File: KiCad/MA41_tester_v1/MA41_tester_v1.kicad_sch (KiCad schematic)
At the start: 5 parts

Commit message: ...
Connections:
- net GND: now also A?.29 (GND), J?.1 (Pin_1)
- net MA41_UART_RX: now reaches J?.2 (Pin_2)
- net MA41_UART_TX: now reaches J?.3 (Pin_3)
- net +3.3V: now reaches J?.4 (Pin_4)
- net MA-41/VCC: now reaches A?.27 (+5V)
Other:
- sheet LCD ports: added GND, SCL, SDA, VCC; removed none
- sheet MA-41 ports: added 3.3V, GND, UART_RX, UART_TX, VCC; removed none
- moved on the sheet: A?, J?, R?

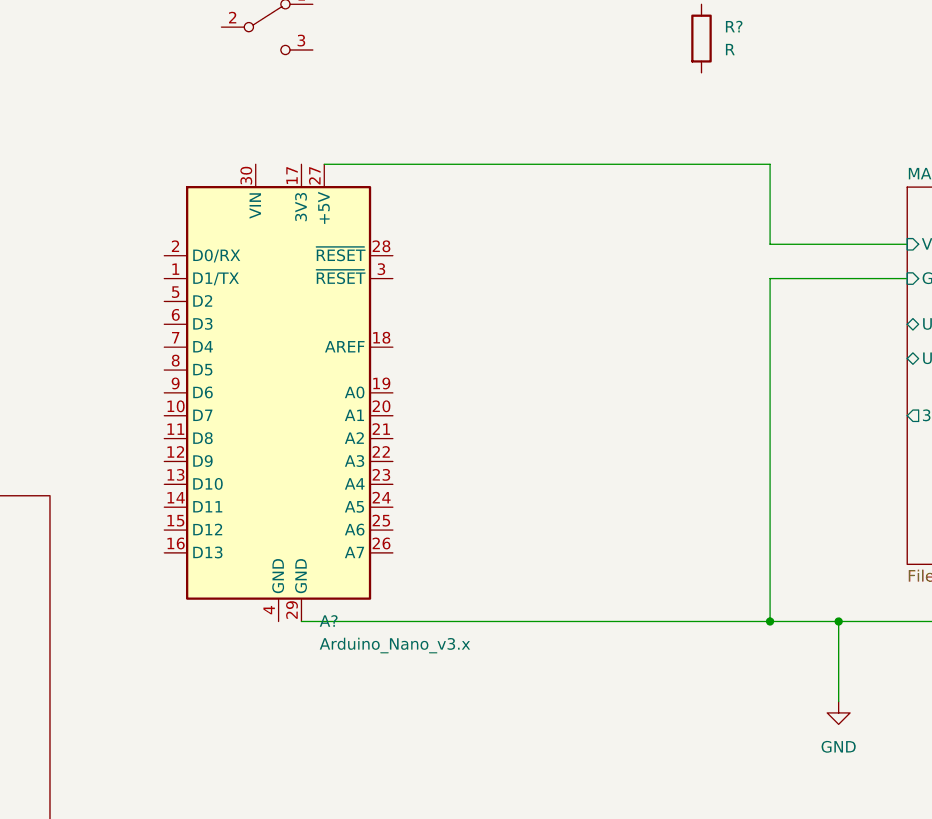
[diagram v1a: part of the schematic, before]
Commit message: arduino changed to esp32
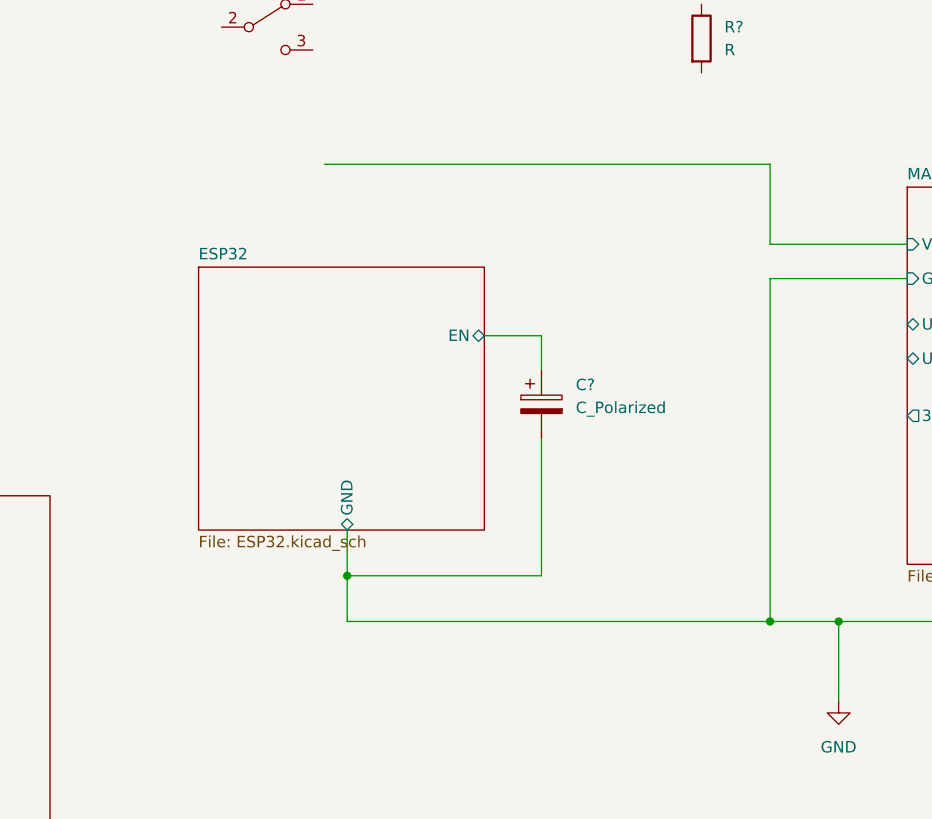
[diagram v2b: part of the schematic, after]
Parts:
- removed A?: Arduino_Nano_v3.x, Module:Arduino_Nano, symbol MCU_Module:Arduino_Nano_v3.x
- added C?: C_Polarized, symbol Device:C_Polarized
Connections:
- net GND: now also C?.2
- new net ESP32/EN: C?.1
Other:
- added sheet ESP32 (ESP32.kicad_sch)
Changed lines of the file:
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@@
   (junction (at 171.45 116.84) (diameter 0) (color 0 0 0 0)
   )
+  (junction (at 124.46 111.76) (diameter 0) (color 0 0 0 0)
+  )
   (junction (at 242.57 81.28) (diameter 0) (color 0 0 0 0)
   )
@@
     (stroke (width 0) (type default) (color 0 0 0 0))
   )
+  (wire (pts (xy 124.46 106.68) (xy 124.46 111.76))
+    (stroke (width 0) (type default) (color 0 0 0 0))
+  )
   (wire (pts (xy 251.46 80.01) (xy 251.46 78.74))
     (stroke (width 0) (type default) (color 0 0 0 0))
   )
+  (wire (pts (xy 124.46 111.76) (xy 124.46 116.84))
+    (stroke (width 0) (type default) (color 0 0 0 0))
+  )
   (wire (pts (xy 262.89 68.58) (xy 250.19 68.58))
     (stroke (width 0) (type default) (color 0 0 0 0))
@@
     (stroke (width 0) (type default) (color 0 0 0 0))
   )
+  (wire (pts (xy 139.7 85.09) (xy 146.05 85.09))
+    (stroke (width 0) (type default) (color 0 0 0 0))
+  )
   (wire (pts (xy 251.46 78.74) (xy 242.57 78.74))
     (stroke (width 0) (type default) (color 0 0 0 0))
@@
     (stroke (width 0) (type default) (color 0 0 0 0))
   )
+  (wire (pts (xy 146.05 96.52) (xy 146.05 111.76))
+    (stroke (width 0) (type default) (color 0 0 0 0))
+  )
+  (wire (pts (xy 146.05 111.76) (xy 124.46 111.76))
+    (stroke (width 0) (type default) (color 0 0 0 0))
+  )
   (wire (pts (xy 232.41 81.28) (xy 232.41 116.84))
     (stroke (width 0) (type default) (color 0 0 0 0))
@@
     (stroke (width 0) (type default) (color 0 0 0 0))
   )
-  (wire (pts (xy 119.38 116.84) (xy 171.45 116.84))
-    (stroke (width 0) (type default) (color 0 0 0 0))
-  )
   (wire (pts (xy 171.45 116.84) (xy 171.45 78.74))
     (stroke (width 0) (type default) (color 0 0 0 0))
@@
     (stroke (width 0) (type default) (color 0 0 0 0))
   )
+  (wire (pts (xy 146.05 85.09) (xy 146.05 88.9))
+    (stroke (width 0) (type default) (color 0 0 0 0))
+  )
   (wire (pts (xy 242.57 81.28) (xy 232.41 81.28))
+    (stroke (width 0) (type default) (color 0 0 0 0))
+  )
+  (wire (pts (xy 124.46 116.84) (xy 171.45 116.84))
     (stroke (width 0) (type default) (color 0 0 0 0))
   )
@@
     (pin "3")
   )
+  (symbol (lib_id "Device:C_Polarized") (at 146.05 92.71 0) (unit 1)
+    (in_bom yes) (on_board yes) (fields_autoplaced)
+    (property "Reference" "C?" (id 0) (at 149.86 90.5509 0)
+      (effects (font (size 1.27 1.27)) (justify left))
+    )
+    (property "Value" "C_Polarized" (id 1) (at 149.86 93.0909 0)
+      (effects (font (size 1.27 1.27)) (justify left))
+    )
+    (property "Footprint" "" (id 2) (at 147.0152 96.52 0)
+      (effects (font (size 1.27 1.27)) hide)
+    )
+    (property "Datasheet" "~" (id 3) (at 146.05 92.71 0)
+      (effects (font (size 1.27 1.27)) hide)
+    )
+    (pin "1")
+    (pin "2")
+  )
   (symbol (lib_id "Device:R") (at 163.83 52.07 0) (unit 1)
     (in_bom yes) (on_board yes) (fields_autoplaced)
@@
     (pin "2")
   )
-  (symbol (lib_id "MCU_Module:Arduino_Nano_v3.x") (at 116.84 91.44 0) (unit 1)
-    (in_bom yes) (on_board yes) (fields_autoplaced)
-    (property "Reference" "A?" (id 0) (at 121.3994 116.84 0)
-      (effects (font (size 1.27 1.27)) (justify left))
-    )
-    (property "Value" "Arduino_Nano_v3.x" (id 1) (at 121.3994 119.38 0)
-      (effects (font (size 1.27 1.27)) (justify left))
-    )
-    (property "Footprint" "Module:Arduino_Nano" (id 2) (at 116.84 91.44 0)
-      (effects (font (size 1.27 1.27) italic) hide)
-    )
-    (property "Datasheet" "http://www.mouser.com/pdfdocs/Gravitech_Arduino_Nano3_0.pdf" (id 3) (at 116.84 91.44 0)
-      (effects (font (size 1.27 1.27)) hide)
-    )
-    (pin "1")
-    (pin "10")
-    (pin "11")
-    (pin "12")
-    (pin "13")
-    (pin "14")
-    (pin "15")
-    (pin "16")
-    (pin "17")
-    (pin "18")
-    (pin "19")
-    (pin "2")
-    (pin "20")
-    (pin "21")
-    (pin "22")
-    (pin "23")
-    (pin "24")
-    (pin "25")
-    (pin "26")
-    (pin "27")
-    (pin "28")
-    (pin "29")
-    (pin "3")
-    (pin "30")
-    (pin "4")
-    (pin "5")
-    (pin "6")
-    (pin "7")
-    (pin "8")
-    (pin "9")
+  (sheet (at 107.95 77.47) (size 31.75 29.21) (fields_autoplaced)
+    (stroke (width 0.1524) (type solid) (color 0 0 0 0))
+    (fill (color 0 0 0 0.0000))
+    (property "Sheet name" "ESP32" (id 0) (at 107.95 76.7584 0)
+      (effects (font (size 1.27 1.27)) (justify left bottom))
+    )
+    (property "Sheet file" "ESP32.kicad_sch" (id 1) (at 107.95 107.2646 0)
+      (effects (font (size 1.27 1.27)) (justify left top))
+    )
+    (pin "EN" bidirectional (at 139.7 85.09 0)
+      (effects (font (size 1.27 1.27)) (justify right))
+    )
+    (pin "GND" bidirectional (at 124.46 106.68 270)
+      (effects (font (size 1.27 1.27)) (justify left))
+    )
   )
   (sheet (at 186.69 68.58) (size 29.21 41.91) (fields_autoplaced)
@@
     (path "/ec9ad0ca-c047-4fdf-90a6-0d80c2e2fb95" (page "2"))
     (path "/c0024dd4-f568-4a9d-af4a-b140e2a5476d" (page "3"))
+    (path "/0079f128-ad52-4f7c-b867-0c198ef9053a" (page "4"))
   )
   (symbol_instances
@@
       (reference "#PWR?") (unit 1) (value "GND") (footprint "")
     )
-    (path "/f449bd37-cc90-4487-aee6-2a20b8d2843a"
-      (reference "A?") (unit 1) (value "Arduino_Nano_v3.x") (footprint "Module:Arduino_Nano")
+    (path "/2648508c-1099-4ff7-b09b-1f9b78c989ed"
+      (reference "C?") (unit 1) (value "C_Polarized") (footprint "")
     )
     (path "/06afc5ac-4a85-4611-a646-d14679941fba"

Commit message: ююю
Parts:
- added J?: PHR4, symbol Connector:Conn_01x04_Female
- C?: value C_Polarized -> 10 мкФ
- J?: value Conn_01x04_Male -> B4B
- R?: value R -> 5,1 Ом
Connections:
- net +3.3V: now also J?.1 (Pin_1); no longer J?.4 (Pin_4)
- net GND: now also R?.1, SW?.2, SW?.3 (C), J?.4 (Pin_4); no longer J?.1 (Pin_1)
- net MA41_UART_RX: now also J?.3 (Pin_3); no longer J?.2 (Pin_2)
- net MA41_UART_TX: now also J?.2 (Pin_2); no longer J?.3 (Pin_3)
- net ESP32/18: now reaches SW?.2 (B)
- net ESP32/36(VP): now reaches R?.2
- net ESP32/36(VP): now also J?.4 (Pin_4)
- net ESP32/19: now reaches SW?.1
- new net ESP32/+3.3V: J?.1 (Pin_1)
- new net ESP32/1(UART0TX): J?.3 (Pin_3)
- new net ESP32/3(UART0RX): J?.2 (Pin_2)
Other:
- sheet ESP32 ports: added +3.3V, 1(UART0TX), 16(UART2RX), 17(UART2TX), 18, 19, 21 SDA, 22 SCL, 3(UART0RX), 36(VP), GND2, Vin; removed none
- sheet MA-41 ports: added NU; removed 3.3V
- note added: "USB"
- moved on the sheet: C?, J?, R?, SW?

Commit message: ///
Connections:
- net ESP32/1(UART0TX): no longer J?.3 (Pin_3)
- net ESP32/3(UART0RX): no longer J?.2 (Pin_2)
- new net ESP32/32: J?.2 (Pin_2)
- new net ESP32/33: J?.3 (Pin_3)
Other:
- sheet ESP32 ports: added 32, 33; removed none
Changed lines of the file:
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@@
-    (stroke (width 0) (type default) (color 0 0 0 0))
-  )
-  (wire (pts (xy 133.35 58.42) (xy 52.07 58.42))
     (stroke (width 0) (type default) (color 0 0 0 0))
   )
@@
     (stroke (width 0) (type default) (color 0 0 0 0))
   )
-  (wire (pts (xy 52.07 58.42) (xy 52.07 46.99))
-    (stroke (width 0) (type default) (color 0 0 0 0))
-  )
   (wire (pts (xy 54.61 36.83) (xy 59.69 36.83))
     (stroke (width 0) (type default) (color 0 0 0 0))
@@
     (stroke (width 0) (type default) (color 0 0 0 0))
   )
+  (wire (pts (xy 76.2 53.34) (xy 49.53 53.34))
+    (stroke (width 0) (type default) (color 0 0 0 0))
+  )
   (wire (pts (xy 153.67 116.84) (xy 153.67 90.17))
     (stroke (width 0) (type default) (color 0 0 0 0))
   )
+  (wire (pts (xy 95.25 105.41) (xy 76.2 105.41))
+    (stroke (width 0) (type default) (color 0 0 0 0))
+  )
   (wire (pts (xy 100.33 128.27) (xy 128.27 128.27))
     (stroke (width 0) (type default) (color 0 0 0 0))
@@
     (stroke (width 0) (type default) (color 0 0 0 0))
   )
-  (wire (pts (xy 130.81 60.96) (xy 130.81 93.98))
+  (wire (pts (xy 95.25 102.87) (xy 78.74 102.87))
     (stroke (width 0) (type default) (color 0 0 0 0))
   )
@@
     (stroke (width 0) (type default) (color 0 0 0 0))
   )
+  (wire (pts (xy 76.2 105.41) (xy 76.2 53.34))
+    (stroke (width 0) (type default) (color 0 0 0 0))
+  )
   (wire (pts (xy 173.99 128.27) (xy 128.27 128.27))
     (stroke (width 0) (type default) (color 0 0 0 0))
@@
     (stroke (width 0) (type default) (color 0 0 0 0))
   )
-  (wire (pts (xy 130.81 60.96) (xy 49.53 60.96))
-    (stroke (width 0) (type default) (color 0 0 0 0))
-  )
   (wire (pts (xy 201.93 139.7) (xy 201.93 133.35))
     (stroke (width 0) (type default) (color 0 0 0 0))
@@
     (stroke (width 0) (type default) (color 0 0 0 0))
   )
+  (wire (pts (xy 78.74 52.07) (xy 52.07 52.07))
+    (stroke (width 0) (type default) (color 0 0 0 0))
+  )
   (wire (pts (xy 21.59 115.57) (xy 34.29 115.57))
     (stroke (width 0) (type default) (color 0 0 0 0))
@@
     (stroke (width 0) (type default) (color 0 0 0 0))
   )
-  (wire (pts (xy 49.53 60.96) (xy 49.53 46.99))
-    (stroke (width 0) (type default) (color 0 0 0 0))
-  )
   (wire (pts (xy 91.44 132.08) (xy 91.44 156.21))
     (stroke (width 0) (type default) (color 0 0 0 0))
@@
     (stroke (width 0) (type default) (color 0 0 0 0))
   )
-  (wire (pts (xy 133.35 58.42) (xy 133.35 96.52))
-    (stroke (width 0) (type default) (color 0 0 0 0))
-  )
   (wire (pts (xy 132.08 132.08) (xy 132.08 115.57))
     (stroke (width 0) (type default) (color 0 0 0 0))
@@
     (stroke (width 0) (type default) (color 0 0 0 0))
   )
+  (wire (pts (xy 78.74 102.87) (xy 78.74 52.07))
+    (stroke (width 0) (type default) (color 0 0 0 0))
+  )
   (wire (pts (xy 252.73 138.43) (xy 252.73 130.81))
     (stroke (width 0) (type default) (color 0 0 0 0))
@@
     (stroke (width 0) (type default) (color 0 0 0 0))
   )
-  (wire (pts (xy 128.27 93.98) (xy 130.81 93.98))
-    (stroke (width 0) (type default) (color 0 0 0 0))
-  )
   (wire (pts (xy 100.33 109.22) (xy 101.6 109.22))
     (stroke (width 0) (type default) (color 0 0 0 0))
@@
     (stroke (width 0) (type default) (color 0 0 0 0))
   )
-  (wire (pts (xy 128.27 96.52) (xy 133.35 96.52))
-    (stroke (width 0) (type default) (color 0 0 0 0))
-  )
   (wire (pts (xy 95.25 97.79) (xy 86.36 97.79))
     (stroke (width 0) (type default) (color 0 0 0 0))
@@
     (stroke (width 0) (type default) (color 0 0 0 0))
   )
+  (wire (pts (xy 52.07 52.07) (xy 52.07 46.99))
+    (stroke (width 0) (type default) (color 0 0 0 0))
+  )
   (wire (pts (xy 143.51 133.35) (xy 143.51 120.65))
+    (stroke (width 0) (type default) (color 0 0 0 0))
+  )
+  (wire (pts (xy 49.53 53.34) (xy 49.53 46.99))
     (stroke (width 0) (type default) (color 0 0 0 0))
   )
@@
       (effects (font (size 1.27 1.27)) (justify right))
     )
-  )
+    (pin "32" input (at 95.25 102.87 180)
+      (effects (font (size 1.27 1.27)) (justify left))
+    )
+    (pin "33" output (at 95.25 105.41 180)
+      (effects (font (size 1.27 1.27)) (justify left))
+    )
+  )

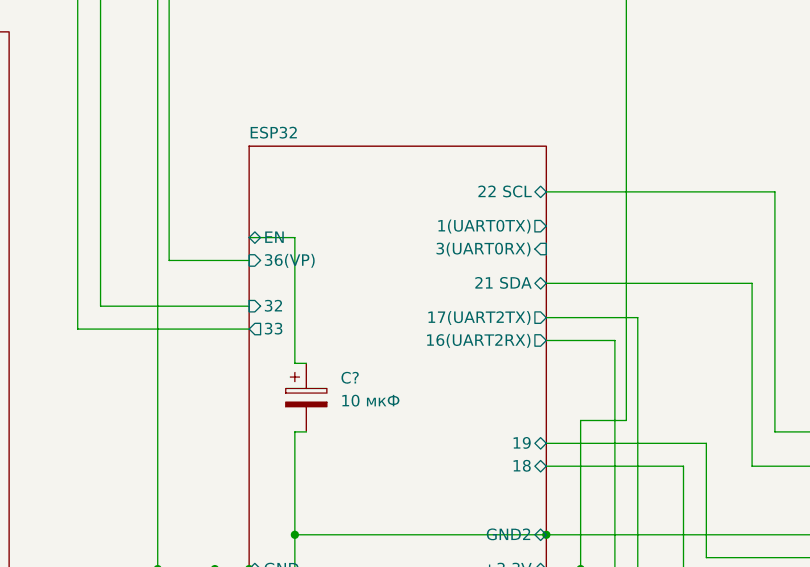
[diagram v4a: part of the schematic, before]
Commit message: fix com port exception
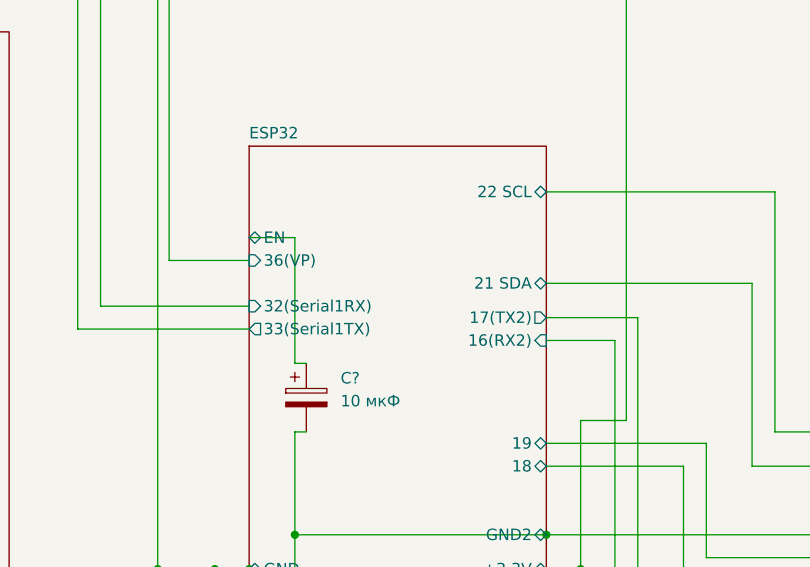
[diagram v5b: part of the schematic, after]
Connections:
- net ESP32/32 renamed ESP32/32(Serial1RX)
- net ESP32/33 renamed ESP32/33(Serial1TX)
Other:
- sheet ESP32 ports: added 16(RX2), 17(TX2), 32(Serial1RX), 33(Serial1TX); removed 1(UART0TX), 16(UART2RX), 17(UART2TX), 3(UART0RX), 32, 33
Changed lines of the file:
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@@
       (effects (font (size 1.27 1.27)) (justify left))
     )
-    (pin "1(UART0TX)" output (at 128.27 93.98 0)
+    (pin "17(TX2)" output (at 128.27 104.14 0)
       (effects (font (size 1.27 1.27)) (justify right))
     )
-    (pin "3(UART0RX)" input (at 128.27 96.52 0)
-      (effects (font (size 1.27 1.27)) (justify right))
-    )
-    (pin "17(UART2TX)" output (at 128.27 104.14 0)
-      (effects (font (size 1.27 1.27)) (justify right))
-    )
-    (pin "16(UART2RX)" output (at 128.27 106.68 0)
+    (pin "16(RX2)" input (at 128.27 106.68 0)
       (effects (font (size 1.27 1.27)) (justify right))
     )
@@
       (effects (font (size 1.27 1.27)) (justify right))
     )
-    (pin "32" input (at 95.25 102.87 180)
+    (pin "32(Serial1RX)" input (at 95.25 102.87 180)
       (effects (font (size 1.27 1.27)) (justify left))
     )
-    (pin "33" output (at 95.25 105.41 180)
+    (pin "33(Serial1TX)" output (at 95.25 105.41 180)
       (effects (font (size 1.27 1.27)) (justify left))
     )
